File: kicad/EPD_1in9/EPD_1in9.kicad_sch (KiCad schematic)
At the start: 12 parts, among them J1 Conn_01x02, J2 Conn_01x08, J3 Conn_01x08, J4 Conn_01x08

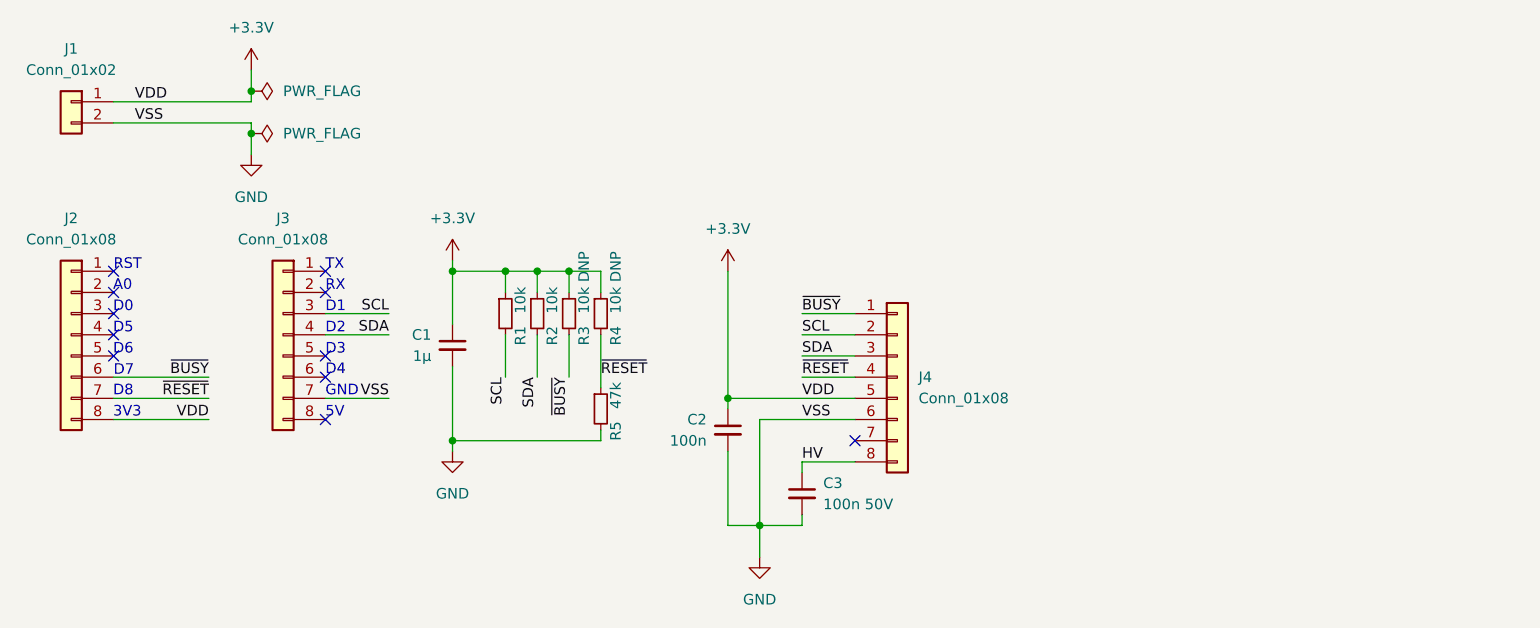
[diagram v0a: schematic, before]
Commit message: EPD_1in9: Add custom footprint for CivLux CF3508
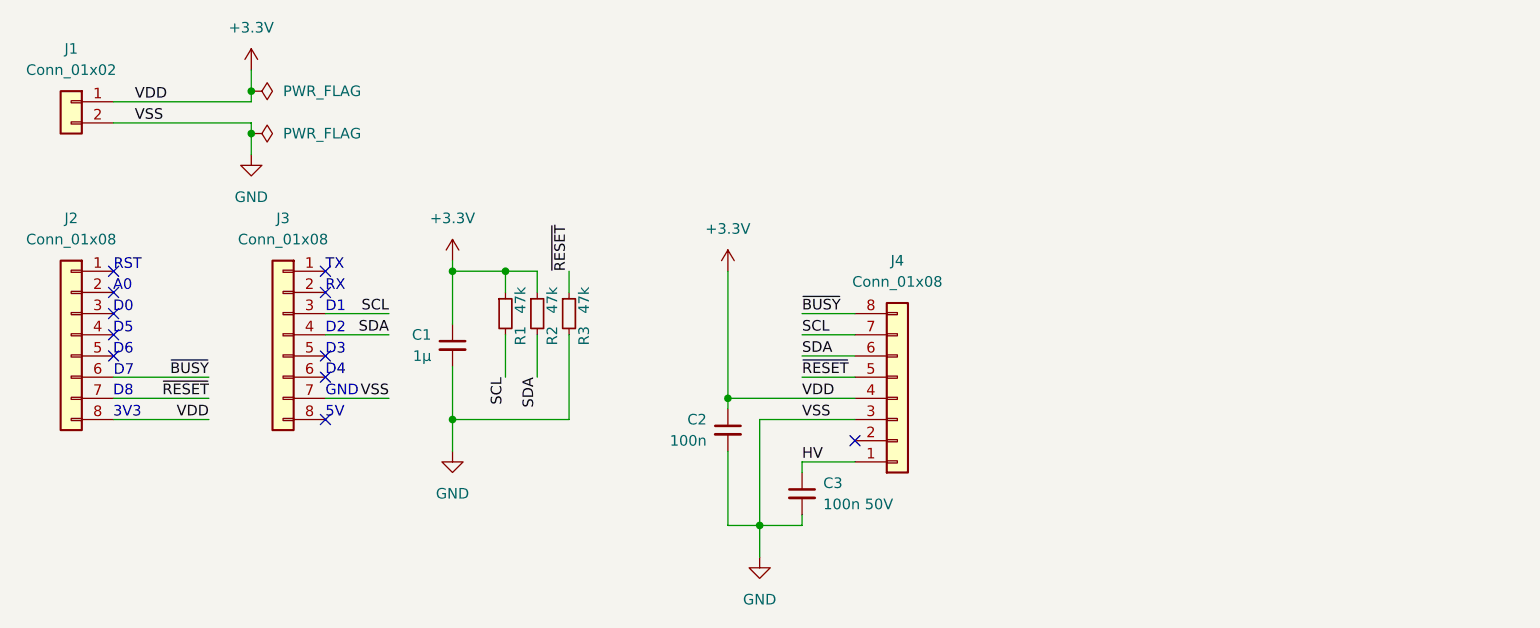
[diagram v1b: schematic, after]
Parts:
- removed R3, R4: 10k DNP, Resistor_SMD:R_0603_1608Metric_Pad0.98x0.95mm_HandSolder, symbol Device:R_Small
- J4: footprint Connector_FFC-FPC:Hirose_FH12-8S-0.5SH_1x08-1MP_P0.50mm_Horizontal -> Connector:CivLux_CF35_1x08-1MP_P0.50mm_Horizontal
- R1, R2: value 10k -> 47k; footprint Resistor_SMD:R_0603_1608Metric_Pad0.98x0.95mm_HandSolder -> Resistor_SMD:R_1206_3216Metric_Pad1.30x1.75mm_HandSolder
- renumbered R5 to R3
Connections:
- net +3.3V: now also J4.4 (Pin_4); no longer J4.5 (Pin_5)
- net GND: now also J4.3 (Pin_3); no longer J4.6 (Pin_6)
- net HV: now also J4.1 (Pin_1); no longer J4.8 (Pin_8)
- net SCL: now also J4.7 (Pin_7); no longer J4.2 (Pin_2)
- net SDA: now also J4.6 (Pin_6); no longer J4.3 (Pin_3)
- net ~{BUSY}: now also J4.8 (Pin_8); no longer J4.1 (Pin_1)
- net ~{RESET}: now also J4.5 (Pin_5); no longer J4.4 (Pin_4)
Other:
- moved on the sheet: R3

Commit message: EPD_1in9: Create board layout for D1 mini adapter board
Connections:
- net +3.3V: now also J1.2 (Pin_2); no longer J1.1 (Pin_1)
- net GND: now also J1.1 (Pin_1); no longer J1.2 (Pin_2)
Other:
- moved on the sheet: J1
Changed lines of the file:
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@@
     (pin "1")
   )
-  (symbol (lib_id "Connector_Generic:Conn_01x02") (at 25.4 25.4 0) (mirror y) (unit 1)
+  (symbol (lib_id "Connector_Generic:Conn_01x02") (at 25.4 27.94 180) (unit 1)
     (in_bom yes) (on_board yes) (fields_autoplaced)
     (property "Reference" "J1" (id 0) (at 25.4 19.05 0))
     (property "Value" "Conn_01x02" (id 1) (at 25.4 21.59 0))
-    (property "Footprint" "Connector_PinHeader_2.54mm:PinHeader_1x02_P2.54mm_Horizontal" (id 2) (at 25.4 25.4 0)
+    (property "Footprint" "Connector_PinHeader_2.54mm:PinHeader_1x02_P2.54mm_Horizontal" (id 2) (at 25.4 27.94 0)
       (effects (font (size 1.27 1.27)) hide)
     )
-    (property "Datasheet" "~" (id 3) (at 25.4 25.4 0)
+    (property "Datasheet" "~" (id 3) (at 25.4 27.94 0)
       (effects (font (size 1.27 1.27)) hide)
     )

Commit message: EPD_1in9: Add schematic symbol and footprint for the display outline
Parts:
- added Disp1: Waveshare_EPD_1in9, Display_local:Waveshare_EPD_1in9, symbol Display_local:Waveshare_EPD_1in9
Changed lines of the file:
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@@
     (pin "8")
+  )
+  (symbol (lib_id "Display_local:Waveshare_EPD_1in9") (at 139.7 71.12 0) (unit 1)
+    (in_bom yes) (on_board yes) (fields_autoplaced)
+    (property "Reference" "Disp1" (id 0) (at 176.53 46.3549 0)
+      (effects (font (size 1.27 1.27)) (justify left))
+    )
+    (property "Value" "Waveshare_EPD_1in9" (id 1) (at 176.53 48.8949 0)
+      (effects (font (size 1.27 1.27)) (justify left))
+    )
+    (property "Footprint" "Display_local:Waveshare_EPD_1in9" (id 2) (at 157.48 74.93 0)
+      (effects (font (size 1.27 1.27)) hide)
+    )
+    (property "Datasheet" "https://www.waveshare.com/w/upload/5/53/1.9inch_Segment_e-Paper_Specification.pdf" (id 3) (at 139.7 77.47 0)
+      (effects (font (size 1.27 1.27)) hide)
+    )
+    (property "Manufacturer URL" "https://www.waveshare.com/wiki/1.9inch_Segment_e-Paper_Module" (id 4) (at 139.7 80.01 0)
+      (effects (font (size 1.27 1.27)) hide)
+    )
   )
   (symbol (lib_id "power:PWR_FLAG") (at 46.99 29.21 270) (unit 1)
@@
       (reference "C3") (unit 1) (value "100n 50V") (footprint "Capacitor_SMD:C_1206_3216Metric_Pad1.33x1.80mm_HandSolder")
     )
+    (path "/e83a8977-0a2c-45f0-9062-9b7d61d4cff5"
+      (reference "Disp1") (unit 1) (value "Waveshare_EPD_1in9") (footprint "Display_local:Waveshare_EPD_1in9")
+    )
     (path "/566747db-af3a-40e1-bc0e-48ac499886b5"

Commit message: EPD_1in9: Add 3D-model for CF3527S connector
IGES model downloaded from:
https://www.cvilux.com/uploads/3d/101/681/CF35082D0RM_NH.zip

Cleaned up colors in FreeCAD and exported as VRML.

Also updated some of the footprint properties and renamed
from CF35 to CF3527S.
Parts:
- J4: footprint Connector:CivLux_CF35_1x08-1MP_P0.50mm_Horizontal -> Connector_local:CivLux_CF3527S_1x08-1MP_P0.50mm_Horizontal
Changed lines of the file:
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@@
     (property "Reference" "J4" (id 0) (at 124.46 44.45 0))
     (property "Value" "Conn_01x08" (id 1) (at 124.46 46.99 0))
-    (property "Footprint" "Connector:CivLux_CF35_1x08-1MP_P0.50mm_Horizontal" (id 2) (at 124.46 60.96 0)
-      (effects (font (size 1.27 1.27)) hide)
-    )
-    (property "Datasheet" "~" (id 3) (at 124.46 60.96 0)
+    (property "Footprint" "Connector_local:CivLux_CF3527S_1x08-1MP_P0.50mm_Horizontal" (id 2) (at 124.46 60.96 0)
+      (effects (font (size 1.27 1.27)) hide)
+    )
+    (property "Datasheet" "https://www.cvilux.com/uploads/spec/101/681/SPCF053.pdf" (id 3) (at 124.46 60.96 0)
       (effects (font (size 1.27 1.27)) hide)
     )
@@
     )
     (path "/7b5a8b59-0c35-47e6-9253-96dbcd2c4ab5"
-      (reference "J4") (unit 1) (value "Conn_01x08") (footprint "Connector:CivLux_CF35_1x08-1MP_P0.50mm_Horizontal")
+      (reference "J4") (unit 1) (value "Conn_01x08") (footprint "Connector_local:CivLux_CF3527S_1x08-1MP_P0.50mm_Horizontal")
     )
     (path "/9204b8c4-a7e8-40da-90c3-2b7c23d3b503"

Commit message: EPD_1in9: Create Rev C circuit board
Updates based on assembly of Rev A boards
-Add labels for the D1-mini pin headers
-Change pin-headers from THT to SMD
 (Note: the 2 pin horizontal connector doesn't have a proper 3D-model)
-Remove large tracks from 3V3 and GND pads and enable thermal reliefs in
 the filled zones
-Update display footprint to better show where the cable folds on the fab
 layer (this also matches the 3D-model)
-Move FPC connector based on where the cable folds to (this also matches
 the 3D-model of the screen better)
-Increase size of routed slot at bottom of board slightly
-Add keepout zone around the HV nets
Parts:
- J1: footprint Connector_PinHeader_2.54mm:PinHeader_1x02_P2.54mm_Horizontal -> Connector_local:PinHeader_1x02_P2.54mm_Horizontal_SMD
- J2, J3: footprint Connector_PinSocket_2.54mm:PinSocket_1x08_P2.54mm_Vertical -> Connector_PinHeader_2.54mm:PinHeader_1x08_P2.54mm_Vertical_SMD_Pin1Right
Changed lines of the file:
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@@
     (property "Reference" "J1" (id 0) (at 25.4 19.05 0))
     (property "Value" "Conn_01x02" (id 1) (at 25.4 21.59 0))
-    (property "Footprint" "Connector_PinHeader_2.54mm:PinHeader_1x02_P2.54mm_Horizontal" (id 2) (at 25.4 27.94 0)
+    (property "Footprint" "Connector_local:PinHeader_1x02_P2.54mm_Horizontal_SMD" (id 2) (at 25.4 27.94 0)
       (effects (font (size 1.27 1.27)) hide)
     )
@@
     (property "Reference" "J2" (id 0) (at 25.4 39.37 0))
     (property "Value" "Conn_01x08" (id 1) (at 25.4 41.91 0))
-    (property "Footprint" "Connector_PinSocket_2.54mm:PinSocket_1x08_P2.54mm_Vertical" (id 2) (at 25.4 53.34 0)
+    (property "Footprint" "Connector_PinHeader_2.54mm:PinHeader_1x08_P2.54mm_Vertical_SMD_Pin1Right" (id 2) (at 25.4 53.34 0)
       (effects (font (size 1.27 1.27)) hide)
     )
@@
     (property "Reference" "J3" (id 0) (at 50.8 39.37 0))
     (property "Value" "Conn_01x08" (id 1) (at 50.8 41.91 0))
-    (property "Footprint" "Connector_PinSocket_2.54mm:PinSocket_1x08_P2.54mm_Vertical" (id 2) (at 50.8 53.34 0)
+    (property "Footprint" "Connector_PinHeader_2.54mm:PinHeader_1x08_P2.54mm_Vertical_SMD_Pin1Right" (id 2) (at 50.8 53.34 0)
       (effects (font (size 1.27 1.27)) hide)
     )
@@
     )
     (path "/566747db-af3a-40e1-bc0e-48ac499886b5"
-      (reference "J1") (unit 1) (value "Conn_01x02") (footprint "Connector_PinHeader_2.54mm:PinHeader_1x02_P2.54mm_Horizontal")
+      (reference "J1") (unit 1) (value "Conn_01x02") (footprint "Connector_local:PinHeader_1x02_P2.54mm_Horizontal_SMD")
     )
     (path "/ae782f28-1c12-4065-a98a-eee05974f10c"
-      (reference "J2") (unit 1) (value "Conn_01x08") (footprint "Connector_PinSocket_2.54mm:PinSocket_1x08_P2.54mm_Vertical")
+      (reference "J2") (unit 1) (value "Conn_01x08") (footprint "Connector_PinHeader_2.54mm:PinHeader_1x08_P2.54mm_Vertical_SMD_Pin1Right")
     )
     (path "/e226d511-19fc-45da-9fc0-680194ebf1fe"
-      (reference "J3") (unit 1) (value "Conn_01x08") (footprint "Connector_PinSocket_2.54mm:PinSocket_1x08_P2.54mm_Vertical")
+      (reference "J3") (unit 1) (value "Conn_01x08") (footprint "Connector_PinHeader_2.54mm:PinHeader_1x08_P2.54mm_Vertical_SMD_Pin1Right")
     )
     (path "/7b5a8b59-0c35-47e6-9253-96dbcd2c4ab5"

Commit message: EPD_1in9: Create Rev D circuit board
Just switch from right-angle power input header to normal vertical header.
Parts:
- J1: footprint Connector_local:PinHeader_1x02_P2.54mm_Horizontal_SMD -> Connector_PinHeader_2.54mm:PinHeader_1x02_P2.54mm_Vertical_SMD_Pin1Right
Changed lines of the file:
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@@
     (property "Reference" "J1" (id 0) (at 25.4 19.05 0))
     (property "Value" "Conn_01x02" (id 1) (at 25.4 21.59 0))
-    (property "Footprint" "Connector_local:PinHeader_1x02_P2.54mm_Horizontal_SMD" (id 2) (at 25.4 27.94 0)
+    (property "Footprint" "Connector_PinHeader_2.54mm:PinHeader_1x02_P2.54mm_Vertical_SMD_Pin1Right" (id 2) (at 25.4 27.94 0)
       (effects (font (size 1.27 1.27)) hide)
     )
@@
     )
     (path "/566747db-af3a-40e1-bc0e-48ac499886b5"
-      (reference "J1") (unit 1) (value "Conn_01x02") (footprint "Connector_local:PinHeader_1x02_P2.54mm_Horizontal_SMD")
+      (reference "J1") (unit 1) (value "Conn_01x02") (footprint "Connector_PinHeader_2.54mm:PinHeader_1x02_P2.54mm_Vertical_SMD_Pin1Right")
     )
     (path "/ae782f28-1c12-4065-a98a-eee05974f10c"
